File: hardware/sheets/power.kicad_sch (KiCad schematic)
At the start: 25 parts, among them J1 USB_C_Receptacle, U1 CH224K, U2 TPS563200

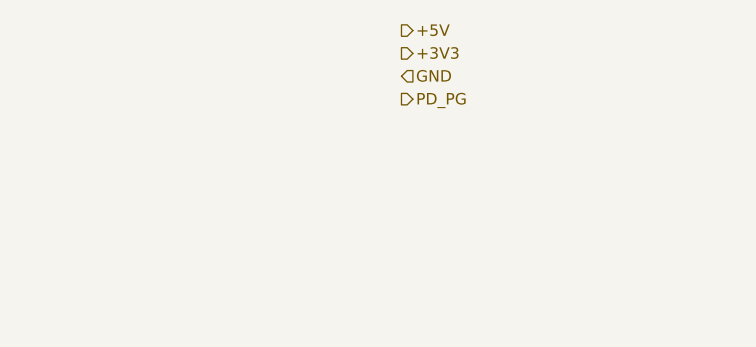
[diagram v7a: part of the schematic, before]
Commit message: ERC cleanup: NC flags on unused pins, anchored interface labels
KiCad 10 ERC drops from 366 to 16 violations, all noise:

- NC flags on the 36 genuinely unused pins (cpu_core '138/'161 spares,
  Supervisor RP2040 unused GPIO, Core2350B GPIO44-47, rtc '138 spares).
- emit_interface anchors every hier label on a stub wire ending in a
  same-name local label -- connectivity unchanged (still by name;
  netlist spans verified), but nothing dangles.
- Interface honesty: cpu_core drops AEN/IOCHRDY from PINS (both live on
  bus_mcu; nothing here touched them), bus_mcu drops PRIV_COUNTER (the
  counter chain is on-sheet, CNT_* never crosses).
- Remaining 6 label_dangling are root IRQ9-13/15: single-sheet by
  design (soft-PIC pull-ups await future 16-bit sources); kept in PINS
  as the AT-style contract.

Co-Authored-By: Claude Fable 5 <noreply@anthropic.com>
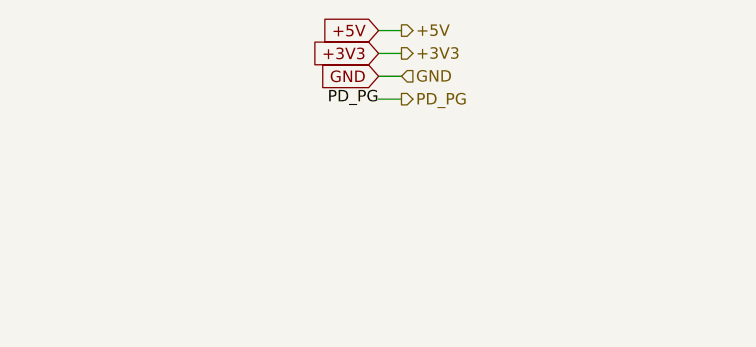
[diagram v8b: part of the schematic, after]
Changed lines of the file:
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@@
 		(company "Andrew C. Young")
 	)
+	(wire
+		(pts
+			(xy 22.86 25.4)
+			(xy 25.4 25.4)
+		)
+		(stroke
+			(width 0)
+			(type default)
+		)
+	)
+	(global_label "+5V"
+		(shape input)
+		(at 22.86 25.4 180)
+		(effects
+			(font
+				(size 1.27 1.27)
+			)
+			(justify right)
+		)
+	)
 	(hierarchical_label "+5V"
 		(shape output)
@@
 		)
 	)
+	(wire
+		(pts
+			(xy 22.86 27.94)
+			(xy 25.4 27.94)
+		)
+		(stroke
+			(width 0)
+			(type default)
+		)
+	)
+	(global_label "+3V3"
+		(shape input)
+		(at 22.86 27.94 180)
+		(effects
+			(font
+				(size 1.27 1.27)
+			)
+			(justify right)
+		)
+	)
 	(hierarchical_label "+3V3"
 		(shape output)
@@
 		)
 	)
+	(wire
+		(pts
+			(xy 22.86 30.48)
+			(xy 25.4 30.48)
+		)
+		(stroke
+			(width 0)
+			(type default)
+		)
+	)
+	(global_label "GND"
+		(shape input)
+		(at 22.86 30.48 180)
+		(effects
+			(font
+				(size 1.27 1.27)
+			)
+			(justify right)
+		)
+	)
 	(hierarchical_label "GND"
 		(shape input)
@@
 		)
 	)
+	(wire
+		(pts
+			(xy 22.86 33.02)
+			(xy 25.4 33.02)
+		)
+		(stroke
+			(width 0)
+			(type default)
+		)
+	)
+	(label "PD_PG"
+		(at 22.86 33.02 180)
+		(effects
+			(font
+				(size 1.27 1.27)
+			)
+			(justify right)
+		)
+	)
 	(hierarchical_label "PD_PG"
 		(shape output)
@@
 		(instances
 			(project "mini-xt"
-				(path "/26736c46-8b40-5460-874f-03596d17270c/68f49a9c-4c78-5695-9186-0a02271fa638"
+				(path "/26736c46-8b40-5460-874f-03596d17270c/a693f317-71cb-5d55-b841-ca6e41b33f1b"
 					(reference "J901")
 					(unit 1)
@@
 		(instances
 			(project "mini-xt"
-				(path "/26736c46-8b40-5460-874f-03596d17270c/68f49a9c-4c78-5695-9186-0a02271fa638"
+				(path "/26736c46-8b40-5460-874f-03596d17270c/a693f317-71cb-5d55-b841-ca6e41b33f1b"
 					(reference "R901")
 					(unit 1)
@@
 		(instances
 			(project "mini-xt"
-				(path "/26736c46-8b40-5460-874f-03596d17270c/68f49a9c-4c78-5695-9186-0a02271fa638"
+				(path "/26736c46-8b40-5460-874f-03596d17270c/a693f317-71cb-5d55-b841-ca6e41b33f1b"
 					(reference "R902")
 					(unit 1)
@@
 		(instances
 			(project "mini-xt"
-				(path "/26736c46-8b40-5460-874f-03596d17270c/68f49a9c-4c78-5695-9186-0a02271fa638"
+				(path "/26736c46-8b40-5460-874f-03596d17270c/a693f317-71cb-5d55-b841-ca6e41b33f1b"
 					(reference "F901")
 					(unit 1)
@@
 		(instances
 			(project "mini-xt"
-				(path "/26736c46-8b40-5460-874f-03596d17270c/68f49a9c-4c78-5695-9186-0a02271fa638"
+				(path "/26736c46-8b40-5460-874f-03596d17270c/a693f317-71cb-5d55-b841-ca6e41b33f1b"
 					(reference "D903")
 					(unit 1)
@@
 		(instances
 			(project "mini-xt"
-				(path "/26736c46-8b40-5460-874f-03596d17270c/68f49a9c-4c78-5695-9186-0a02271fa638"
+				(path "/26736c46-8b40-5460-874f-03596d17270c/a693f317-71cb-5d55-b841-ca6e41b33f1b"
 					(reference "U901")
 					(unit 1)
@@
 		(instances
 			(project "mini-xt"
-				(path "/26736c46-8b40-5460-874f-03596d17270c/68f49a9c-4c78-5695-9186-0a02271fa638"
+				(path "/26736c46-8b40-5460-874f-03596d17270c/a693f317-71cb-5d55-b841-ca6e41b33f1b"
 					(reference "R909")
 					(unit 1)
@@
 		(instances
 			(project "mini-xt"
-				(path "/26736c46-8b40-5460-874f-03596d17270c/68f49a9c-4c78-5695-9186-0a02271fa638"
+				(path "/26736c46-8b40-5460-874f-03596d17270c/a693f317-71cb-5d55-b841-ca6e41b33f1b"
 					(reference "R904")
 					(unit 1)
@@
 		(instances
 			(project "mini-xt"
-				(path "/26736c46-8b40-5460-874f-03596d17270c/68f49a9c-4c78-5695-9186-0a02271fa638"
+				(path "/26736c46-8b40-5460-874f-03596d17270c/a693f317-71cb-5d55-b841-ca6e41b33f1b"
 					(reference "C906")
 					(unit 1)
@@
 		(instances
 			(project "mini-xt"
-				(path "/26736c46-8b40-5460-874f-03596d17270c/68f49a9c-4c78-5695-9186-0a02271fa638"
+				(path "/26736c46-8b40-5460-874f-03596d17270c/a693f317-71cb-5d55-b841-ca6e41b33f1b"
 					(reference "C901")
 					(unit 1)
@@
 		(instances
 			(project "mini-xt"
-				(path "/26736c46-8b40-5460-874f-03596d17270c/68f49a9c-4c78-5695-9186-0a02271fa638"
+				(path "/26736c46-8b40-5460-874f-03596d17270c/a693f317-71cb-5d55-b841-ca6e41b33f1b"
 					(reference "C902")
 					(unit 1)
@@
 		(instances
 			(project "mini-xt"
-				(path "/26736c46-8b40-5460-874f-03596d17270c/68f49a9c-4c78-5695-9186-0a02271fa638"
+				(path "/26736c46-8b40-5460-874f-03596d17270c/a693f317-71cb-5d55-b841-ca6e41b33f1b"
 					(reference "U902")
 					(unit 1)
@@
 		(instances
 			(project "mini-xt"
-				(path "/26736c46-8b40-5460-874f-03596d17270c/68f49a9c-4c78-5695-9186-0a02271fa638"
+				(path "/26736c46-8b40-5460-874f-03596d17270c/a693f317-71cb-5d55-b841-ca6e41b33f1b"
 					(reference "C905")
 					(unit 1)
@@
 		(instances
 			(project "mini-xt"
-				(path "/26736c46-8b40-5460-874f-03596d17270c/68f49a9c-4c78-5695-9186-0a02271fa638"
+				(path "/26736c46-8b40-5460-874f-03596d17270c/a693f317-71cb-5d55-b841-ca6e41b33f1b"
 					(reference "L901")
 					(unit 1)
@@
 		(instances
 			(project "mini-xt"
-				(path "/26736c46-8b40-5460-874f-03596d17270c/68f49a9c-4c78-5695-9186-0a02271fa638"
+				(path "/26736c46-8b40-5460-874f-03596d17270c/a693f317-71cb-5d55-b841-ca6e41b33f1b"
 					(reference "R905")
 					(unit 1)
@@
 		(instances
 			(project "mini-xt"
-				(path "/26736c46-8b40-5460-874f-03596d17270c/68f49a9c-4c78-5695-9186-0a02271fa638"
+				(path "/26736c46-8b40-5460-874f-03596d17270c/a693f317-71cb-5d55-b841-ca6e41b33f1b"
 					(reference "R906")
 					(unit 1)
@@
 		(instances
 			(project "mini-xt"
-				(path "/26736c46-8b40-5460-874f-03596d17270c/68f49a9c-4c78-5695-9186-0a02271fa638"
+				(path "/26736c46-8b40-5460-874f-03596d17270c/a693f317-71cb-5d55-b841-ca6e41b33f1b"
 					(reference "C903")
 					(unit 1)
@@
 		(instances
 			(project "mini-xt"
-				(path "/26736c46-8b40-5460-874f-03596d17270c/68f49a9c-4c78-5695-9186-0a02271fa638"
+				(path "/26736c46-8b40-5460-874f-03596d17270c/a693f317-71cb-5d55-b841-ca6e41b33f1b"
 					(reference "C904")
 					(unit 1)
@@
 		(instances
 			(project "mini-xt"
-				(path "/26736c46-8b40-5460-874f-03596d17270c/68f49a9c-4c78-5695-9186-0a02271fa638"
+				(path "/26736c46-8b40-5460-874f-03596d17270c/a693f317-71cb-5d55-b841-ca6e41b33f1b"
 					(reference "C907")
 					(unit 1)
@@
 		(instances
 			(project "mini-xt"
-				(path "/26736c46-8b40-5460-874f-03596d17270c/68f49a9c-4c78-5695-9186-0a02271fa638"
+				(path "/26736c46-8b40-5460-874f-03596d17270c/a693f317-71cb-5d55-b841-ca6e41b33f1b"
 					(reference "C908")
 					(unit 1)
@@
 		(instances
 			(project "mini-xt"
-				(path "/26736c46-8b40-5460-874f-03596d17270c/68f49a9c-4c78-5695-9186-0a02271fa638"
+				(path "/26736c46-8b40-5460-874f-03596d17270c/a693f317-71cb-5d55-b841-ca6e41b33f1b"
 					(reference "C909")
 					(unit 1)
@@
 		(instances
 			(project "mini-xt"
-				(path "/26736c46-8b40-5460-874f-03596d17270c/68f49a9c-4c78-5695-9186-0a02271fa638"
+				(path "/26736c46-8b40-5460-874f-03596d17270c/a693f317-71cb-5d55-b841-ca6e41b33f1b"
 					(reference "R907")
 					(unit 1)
@@
 		(instances
 			(project "mini-xt"
-				(path "/26736c46-8b40-5460-874f-03596d17270c/68f49a9c-4c78-5695-9186-0a02271fa638"
+				(path "/26736c46-8b40-5460-874f-03596d17270c/a693f317-71cb-5d55-b841-ca6e41b33f1b"
 					(reference "D901")
 					(unit 1)
@@
 		(instances
 			(project "mini-xt"
-				(path "/26736c46-8b40-5460-874f-03596d17270c/68f49a9c-4c78-5695-9186-0a02271fa638"
+				(path "/26736c46-8b40-5460-874f-03596d17270c/a693f317-71cb-5d55-b841-ca6e41b33f1b"
 					(reference "R908")
 					(unit 1)
@@
 		(instances
 			(project "mini-xt"
-				(path "/26736c46-8b40-5460-874f-03596d17270c/68f49a9c-4c78-5695-9186-0a02271fa638"
+				(path "/26736c46-8b40-5460-874f-03596d17270c/a693f317-71cb-5d55-b841-ca6e41b33f1b"
 					(reference "D902")
 					(unit 1)
@@
 		(instances
 			(project "mini-xt"
-				(path "/26736c46-8b40-5460-874f-03596d17270c/68f49a9c-4c78-5695-9186-0a02271fa638"
+				(path "/26736c46-8b40-5460-874f-03596d17270c/a693f317-71cb-5d55-b841-ca6e41b33f1b"
 					(reference "#FLG901")
 					(unit 1)
@@
 		(instances
 			(project "mini-xt"
-				(path "/26736c46-8b40-5460-874f-03596d17270c/68f49a9c-4c78-5695-9186-0a02271fa638"
+				(path "/26736c46-8b40-5460-874f-03596d17270c/a693f317-71cb-5d55-b841-ca6e41b33f1b"
 					(reference "#FLG902")
 					(unit 1)
@@
 		(instances
 			(project "mini-xt"
-				(path "/26736c46-8b40-5460-874f-03596d17270c/68f49a9c-4c78-5695-9186-0a02271fa638"
+				(path "/26736c46-8b40-5460-874f-03596d17270c/a693f317-71cb-5d55-b841-ca6e41b33f1b"
 					(reference "#FLG903")
 					(unit 1)
@@
 		(instances
 			(project "mini-xt"
-				(path "/26736c46-8b40-5460-874f-03596d17270c/68f49a9c-4c78-5695-9186-0a02271fa638"
+				(path "/26736c46-8b40-5460-874f-03596d17270c/a693f317-71cb-5d55-b841-ca6e41b33f1b"
 					(reference "#FLG904")
 					(unit 1)
@@
 		(instances
 			(project "mini-xt"
-				(path "/26736c46-8b40-5460-874f-03596d17270c/68f49a9c-4c78-5695-9186-0a02271fa638"
+				(path "/26736c46-8b40-5460-874f-03596d17270c/a693f317-71cb-5d55-b841-ca6e41b33f1b"
 					(reference "#PWR901")
 					(unit 1)
